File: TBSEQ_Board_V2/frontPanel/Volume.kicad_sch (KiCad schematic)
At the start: 2 parts, among them J1 MJ-462

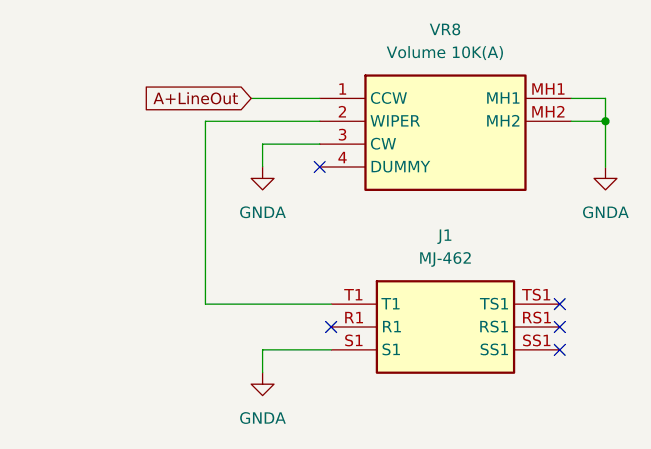
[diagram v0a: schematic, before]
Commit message: AddBoard
Ver3まで登録
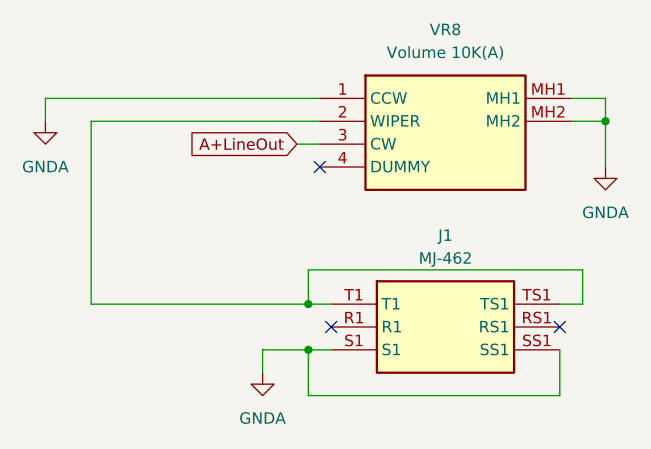
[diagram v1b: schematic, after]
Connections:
- net A+LineOut: now also VR8.3 (CW); no longer VR8.1 (CCW)
- net GNDA: now also J1.SS1, VR8.1 (CCW); no longer VR8.3 (CW)
- net at J1.T1, VR8.2 (WIPER): now also J1.TS1
- no-connect marks 5 -> 3
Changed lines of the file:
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@@
 		(color 0 0 0 0)
 	)
-	(no_connect
-		(at 111.76 72.39)
+	(junction
+		(at 83.82 67.31)
+		(diameter 0)
+		(color 0 0 0 0)
+	)
+	(junction
+		(at 83.82 72.39)
+		(diameter 0)
+		(color 0 0 0 0)
 	)
 	(no_connect
@@
 	)
 	(no_connect
-		(at 111.76 67.31)
-	)
-	(no_connect
 		(at 111.76 69.85)
 	)
@@
 	(wire
 		(pts
-			(xy 85.09 49.53) (xy 78.74 49.53)
+			(xy 59.69 67.31) (xy 83.82 67.31)
+		)
+		(stroke
+			(width 0)
+			(type default)
+		)
+	)
+	(wire
+		(pts
+			(xy 82.55 49.53) (xy 85.09 49.53)
 		)
 		(stroke
@@
 	(wire
 		(pts
-			(xy 86.36 72.39) (xy 78.74 72.39)
-		)
-		(stroke
-			(width 0)
-			(type default)
-		)
-	)
-	(wire
-		(pts
-			(xy 72.39 46.99) (xy 85.09 46.99)
-		)
-		(stroke
-			(width 0)
-			(type default)
-		)
-	)
-	(wire
-		(pts
-			(xy 72.39 67.31) (xy 72.39 46.99)
+			(xy 86.36 72.39) (xy 83.82 72.39)
+		)
+		(stroke
+			(width 0)
+			(type default)
+		)
+	)
+	(wire
+		(pts
+			(xy 85.09 46.99) (xy 59.69 46.99)
 		)
 		(stroke
@@
 	(wire
 		(pts
+			(xy 83.82 67.31) (xy 86.36 67.31)
+		)
+		(stroke
+			(width 0)
+			(type default)
+		)
+	)
+	(wire
+		(pts
 			(xy 116.84 44.45) (xy 116.84 46.99)
 		)
@@
 	(wire
 		(pts
-			(xy 77.47 44.45) (xy 85.09 44.45)
-		)
-		(stroke
-			(width 0)
-			(type default)
-		)
-	)
-	(wire
-		(pts
-			(xy 86.36 67.31) (xy 72.39 67.31)
-		)
-		(stroke
-			(width 0)
-			(type default)
-		)
-	)
-	(wire
-		(pts
 			(xy 116.84 46.99) (xy 116.84 52.07)
 		)
@@
 	(wire
 		(pts
-			(xy 78.74 49.53) (xy 78.74 52.07)
+			(xy 114.3 63.5) (xy 114.3 67.31)
+		)
+		(stroke
+			(width 0)
+			(type default)
+		)
+	)
+	(wire
+		(pts
+			(xy 54.61 44.45) (xy 85.09 44.45)
+		)
+		(stroke
+			(width 0)
+			(type default)
+		)
+	)
+	(wire
+		(pts
+			(xy 111.76 77.47) (xy 83.82 77.47)
+		)
+		(stroke
+			(width 0)
+			(type default)
+		)
+	)
+	(wire
+		(pts
+			(xy 59.69 46.99) (xy 59.69 67.31)
+		)
+		(stroke
+			(width 0)
+			(type default)
+		)
+	)
+	(wire
+		(pts
+			(xy 83.82 77.47) (xy 83.82 72.39)
+		)
+		(stroke
+			(width 0)
+			(type default)
+		)
+	)
+	(wire
+		(pts
+			(xy 114.3 67.31) (xy 111.76 67.31)
+		)
+		(stroke
+			(width 0)
+			(type default)
+		)
+	)
+	(wire
+		(pts
+			(xy 83.82 63.5) (xy 114.3 63.5)
+		)
+		(stroke
+			(width 0)
+			(type default)
+		)
+	)
+	(wire
+		(pts
+			(xy 83.82 67.31) (xy 83.82 63.5)
+		)
+		(stroke
+			(width 0)
+			(type default)
+		)
+	)
+	(wire
+		(pts
+			(xy 54.61 46.99) (xy 54.61 44.45)
 		)
 		(stroke
@@
 		(pts
 			(xy 113.03 44.45) (xy 116.84 44.45)
+		)
+		(stroke
+			(width 0)
+			(type default)
+		)
+	)
+	(wire
+		(pts
+			(xy 83.82 72.39) (xy 78.74 72.39)
+		)
+		(stroke
+			(width 0)
+			(type default)
+		)
+	)
+	(wire
+		(pts
+			(xy 111.76 72.39) (xy 111.76 77.47)
 		)
 		(stroke
@@
 	(global_label "A+LineOut"
 		(shape input)
-		(at 77.47 44.45 180)
+		(at 82.55 49.53 180)
 		(fields_autoplaced yes)
 		(effects
@@
 		)
 		(property "Intersheetrefs" "${INTERSHEET_REFS}"
-			(at 64.7481 44.45 0)
+			(at 69.8281 49.53 0)
 			(effects
 				(font
@@
 	(symbol
 		(lib_id "power:GNDA")
-		(at 78.74 52.07 0)
+		(at 54.61 46.99 0)
 		(unit 1)
 		(exclude_from_sim no)
@@
 		(fields_autoplaced yes)
 		(property "Reference" "#PWR05"
-			(at 78.74 58.42 0)
+			(at 54.61 53.34 0)
 			(effects
 				(font
@@
 		)
 		(property "Value" "GNDA"
-			(at 78.74 57.15 0)
+			(at 54.61 52.07 0)
 			(effects
 				(font
@@
 		)
 		(property "Footprint" ""
-			(at 78.74 52.07 0)
+			(at 54.61 46.99 0)
 			(effects
 				(font
@@
 		)
 		(property "Datasheet" ""
-			(at 78.74 52.07 0)
+			(at 54.61 46.99 0)
 			(effects
 				(font
@@
 		)
 		(property "Description" "Power symbol creates a global label with name \"GNDA\" , analog ground"
-			(at 78.74 52.07 0)
-			(effects
-				(font
+			(at 54.61 46.99 0)
+			(effects
+				(font
